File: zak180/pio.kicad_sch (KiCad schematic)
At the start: 4 parts, among them J2 DB25_Receptacle_MountingHoles, U2 PIO-DIP-40

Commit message: HW: Further work on schematic
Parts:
- removed RN2: 47K, Resistor_THT:R_Array_SIP9, symbol Device:R_Network08
- added C22: 100n, Capacitor_THT:C_Disc_D5.0mm_W2.5mm_P2.50mm, symbol Device:C
- added R10, R11, R12, R13, R14, R15, R16, R17, R18, R19, R20, R21, R22, R23, R24, R25, R6, R7, R8, R9: 100R, Resistor_THT:R_Axial_DIN0207_L6.3mm_D2.5mm_P7.62mm_Horizontal, symbol Device:R
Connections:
- net GND: now also C22.2; no longer J2.14 (P14), J2.15 (P15), J2.16 (P16), J2.17 (P17), J2.18 (P18), J2.19 (P19), J2.20 (P20), J2.21 (P21), J2.22 (P22), J2.23 (P23), J2.24 (P24)
- net VCC: now also J2.14 (P14), C22.1
- net at J2.10: now also R19.2; no longer U2.18 (ARDY)
- net at J2.11: now also R23.2; no longer U2.16 (~{ASTB})
- net at J2.2: now also R16.2; no longer U2.15 (PA0)
- net at J2.3: now also R20.2; no longer U2.14 (PA1)
- net at U2.13 (PA2): now also R8.1; no longer J2.4
- net at J2.5: now also R17.2; no longer U2.12 (PA3)
- net at J2.6: now also R21.2; no longer U2.10 (PA4)
- net at U2.9 (PA5): now also R11.1; no longer J2.7
- net at J2.8: now also R18.2; no longer U2.8 (PA6)
- net at J2.9: now also R22.2; no longer U2.7 (PA7)
- net at U2.17 (~{BSTB}): now also R23.1
- net at U2.21 (BRDY): now also R19.1
- net at U2.33 (PB6): now also R18.1
- net at U2.34 (PB7): now also R22.1
- net SCRL0: no longer names the net of U2.27 (PB0)
- net SCRL0: now also R16.1
- net SCRL1: no longer names the net of U2.28 (PB1)
- net SCRL1: now also R20.1
- net SCRL2: no longer names the net of U2.29 (PB2)
- net SCRL2: now also R24.1
- net SCRL3: no longer names the net of U2.30 (PB3)
- net SCRL3: now also R17.1
- net SCRL4: no longer names the net of U2.31 (PB4)
- net SCRL4: now also R21.1
- net SCRL5: no longer names the net of U2.32 (PB5)
- net SCRL5: now also R25.1
- new net: J2.20 (P20), R11.2
- new net: J2.17 (P17), R8.2
- new net: J2.15 (P15), R6.2
- new net: J2.16 (P16), R7.2
- new net: J2.18 (P18), R9.2
- new net: J2.19 (P19), R10.2
- new net: J2.21 (P21), R12.2
- new net: J2.22 (P22), R13.2
- new net: J2.23 (P23), R14.2
- new net: J2.24 (P24), R15.2
- new net: J2.4, R24.2
- new net: J2.7, R25.2
- new net: R13.1, U2.7 (PA7)
- new net: R10.1, U2.10 (PA4)
- new net: R9.1, U2.12 (PA3)
- new net: R7.1, U2.14 (PA1)
- new net: R6.1, U2.15 (PA0)
- new net: R15.1, U2.16 (~{ASTB})
- new net: R14.1, U2.18 (ARDY)
- new net: R12.1, U2.8 (PA6)
- no-connect marks 2 -> 0
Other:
- moved on the sheet: J2

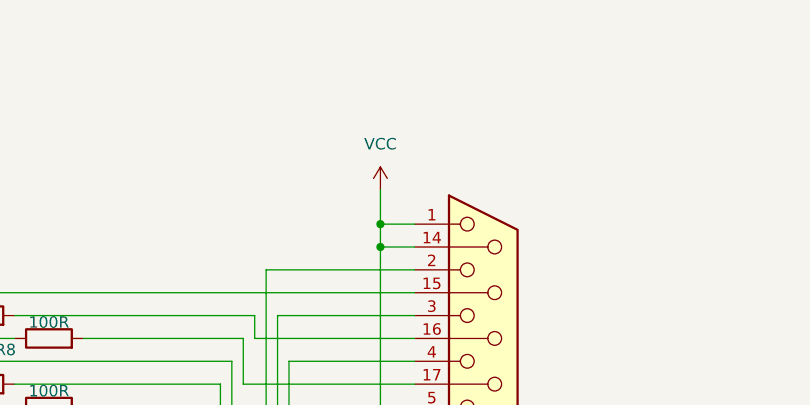
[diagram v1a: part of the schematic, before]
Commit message: HW: Add memory, serial and power
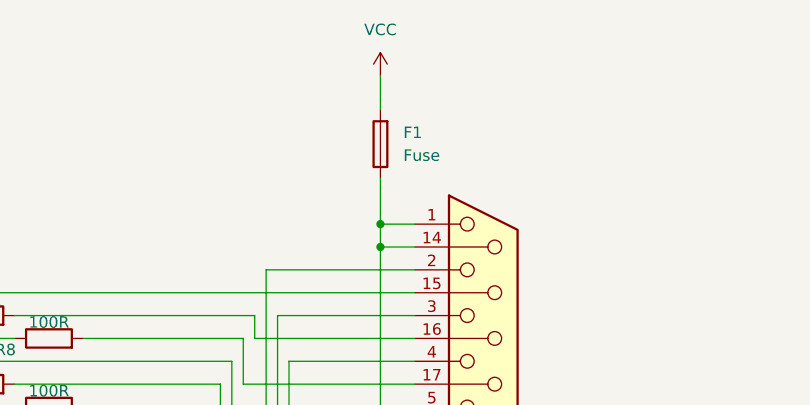
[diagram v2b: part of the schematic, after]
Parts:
- added F1: Fuse, PCM_Fuse_AKL:Fuse_Littelfuse_395Series, symbol Device:Fuse
- J2: footprint (none) -> Connector_Dsub:DSUB-25_Female_Horizontal_P2.77x2.84mm_EdgePinOffset9.90mm_Housed_MountingHolesOffset11.32mm
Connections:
- net VCC: now also F1.2; no longer J2.1, J2.13, J2.14 (P14)
- new net: F1.1, J2.1, J2.13, J2.14 (P14)
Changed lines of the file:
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@@
 	)
 	(junction
-		(at 196.85 58.42)
+		(at 196.85 60.96)
 		(diameter 0)
 		(color 0 0 0 0)
 	)
 	(junction
-		(at 196.85 60.96)
+		(at 196.85 58.42)
 		(diameter 0)
 		(color 0 0 0 0)
@@
 	(wire
 		(pts
-			(xy 196.85 54.61) (xy 196.85 58.42)
-		)
-		(stroke
-			(width 0)
-			(type default)
-		)
-	)
-	(wire
-		(pts
 			(xy 196.85 58.42) (xy 196.85 60.96)
 		)
@@
 	(wire
 		(pts
+			(xy 196.85 41.91) (xy 196.85 45.72)
+		)
+		(stroke
+			(width 0)
+			(type default)
+		)
+	)
+	(wire
+		(pts
 			(xy 208.28 127) (xy 198.12 127)
 		)
@@
 		)
 	)
+	(wire
+		(pts
+			(xy 196.85 53.34) (xy 196.85 58.42)
+		)
+		(stroke
+			(width 0)
+			(type default)
+		)
+	)
 	(bus
 		(pts
@@
 	)
 	(symbol
+		(lib_id "Device:Fuse")
+		(at 196.85 49.53 180)
+		(unit 1)
+		(exclude_from_sim no)
+		(in_bom yes)
+		(on_board yes)
+		(dnp no)
+		(fields_autoplaced yes)
+		(property "Reference" "F1"
+			(at 199.39 48.2599 0)
+			(effects
+				(font
+					(size 1.27 1.27)
+				)
+				(justify right)
+			)
+		)
+		(property "Value" "Fuse"
+			(at 199.39 50.7999 0)
+			(effects
+				(font
+					(size 1.27 1.27)
+				)
+				(justify right)
+			)
+		)
+		(property "Footprint" "PCM_Fuse_AKL:Fuse_Littelfuse_395Series"
+			(at 198.628 49.53 90)
+			(effects
+				(font
+					(size 1.27 1.27)
+				)
+				(hide yes)
+			)
+		)
+		(property "Datasheet" "~"
+			(at 196.85 49.53 0)
+			(effects
+				(font
+					(size 1.27 1.27)
+				)
+				(hide yes)
+			)
+		)
+		(property "Description" "Fuse"
+			(at 196.85 49.53 0)
+			(effects
+				(font
+					(size 1.27 1.27)
+				)
+				(hide yes)
+			)
+		)
+		(pin "1"
+		)
+		(pin "2"
+		)
+		(instances
+			(project "zak180"
+				(path "/ca48b56d-33a4-442b-b1b9-aaf2c2c8d68d/1a7f8631-20f0-471d-ab8f-15a03c343af4"
+					(reference "F1")
+					(unit 1)
+				)
+			)
+		)
+	)
+	(symbol
 		(lib_id "Device:R")
 		(at 152.4 121.92 90)
@@
 			)
 		)
-		(property "Footprint" ""
+		(property "Footprint" "Connector_Dsub:DSUB-25_Female_Horizontal_P2.77x2.84mm_EdgePinOffset9.90mm_Housed_MountingHolesOffset11.32mm"
 			(at 208.28 88.9 0)
 			(effects
@@
 	(symbol
 		(lib_id "power:VCC")
-		(at 196.85 54.61 0)
+		(at 196.85 41.91 0)
 		(unit 1)
 		(exclude_from_sim no)
@@
 		(fields_autoplaced yes)
 		(property "Reference" "#PWR012"
-			(at 196.85 58.42 0)
+			(at 196.85 45.72 0)
 			(effects
 				(font
@@
 		)
 		(property "Value" "VCC"
-			(at 196.85 49.53 0)
+			(at 196.85 36.83 0)
 			(effects
 				(font
@@
 		)
 		(property "Footprint" ""
-			(at 196.85 54.61 0)
+			(at 196.85 41.91 0)
 			(effects
 				(font
@@
 		)
 		(property "Datasheet" ""
-			(at 196.85 54.61 0)
+			(at 196.85 41.91 0)
 			(effects
 				(font
@@
 		)
 		(property "Description" "Power symbol creates a global label with name \"VCC\""
-			(at 196.85 54.61 0)
+			(at 196.85 41.91 0)
 			(effects
 				(font
